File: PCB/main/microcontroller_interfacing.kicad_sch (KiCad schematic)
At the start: 18 parts, among them J5 Conn_01x02_Male, U1 USB_Micro_B, U2 CH340G, U3 AT24C256C-SSHL-T, X1 12MHz Crystal

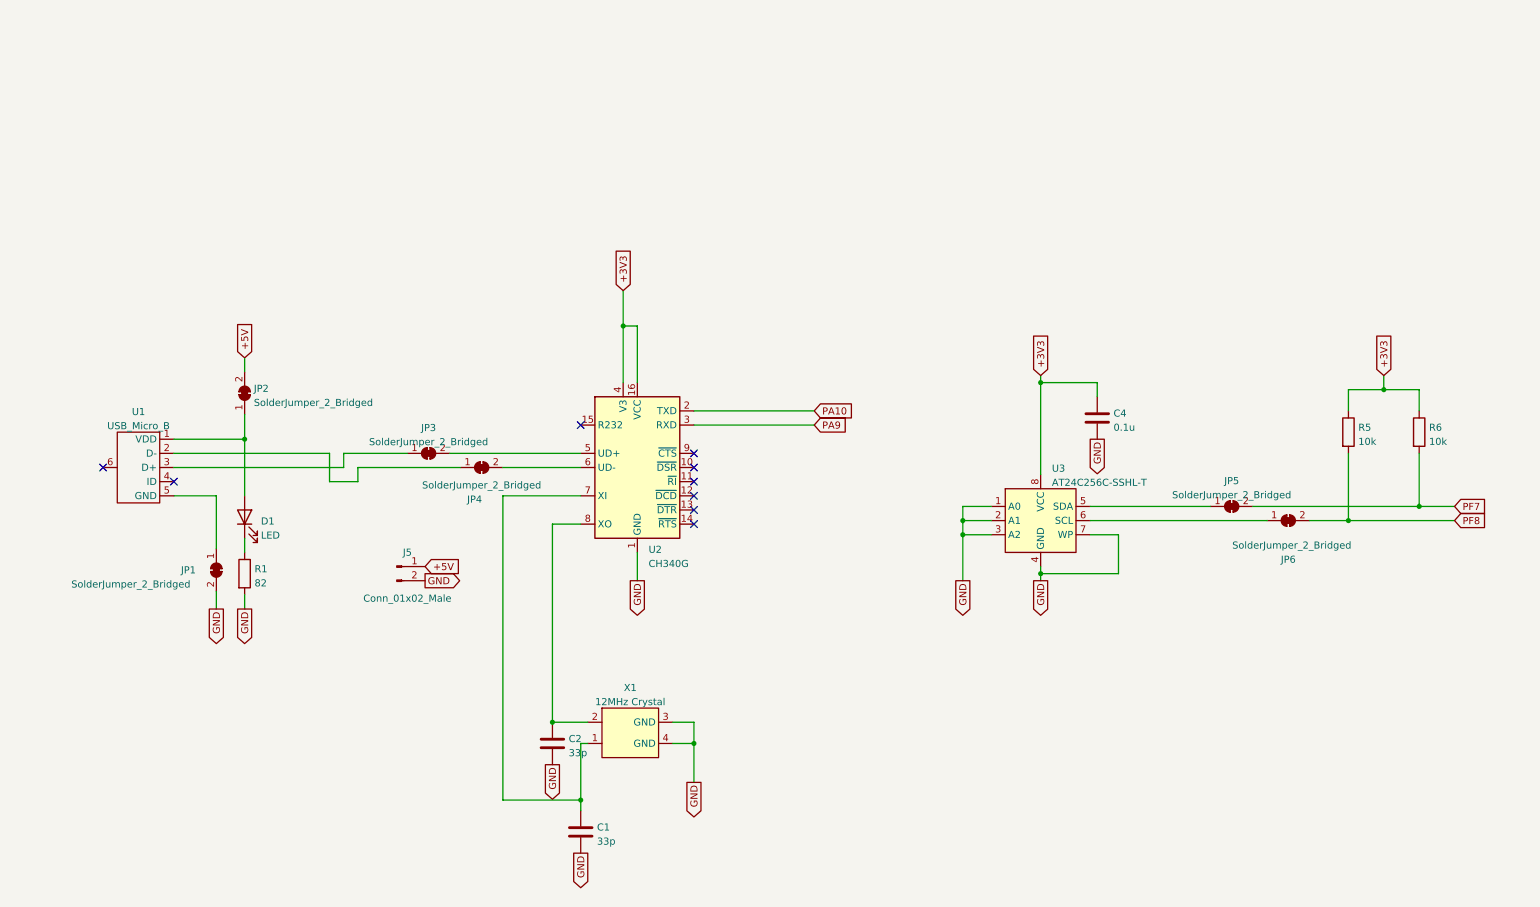
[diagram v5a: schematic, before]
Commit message: Neaten schematic
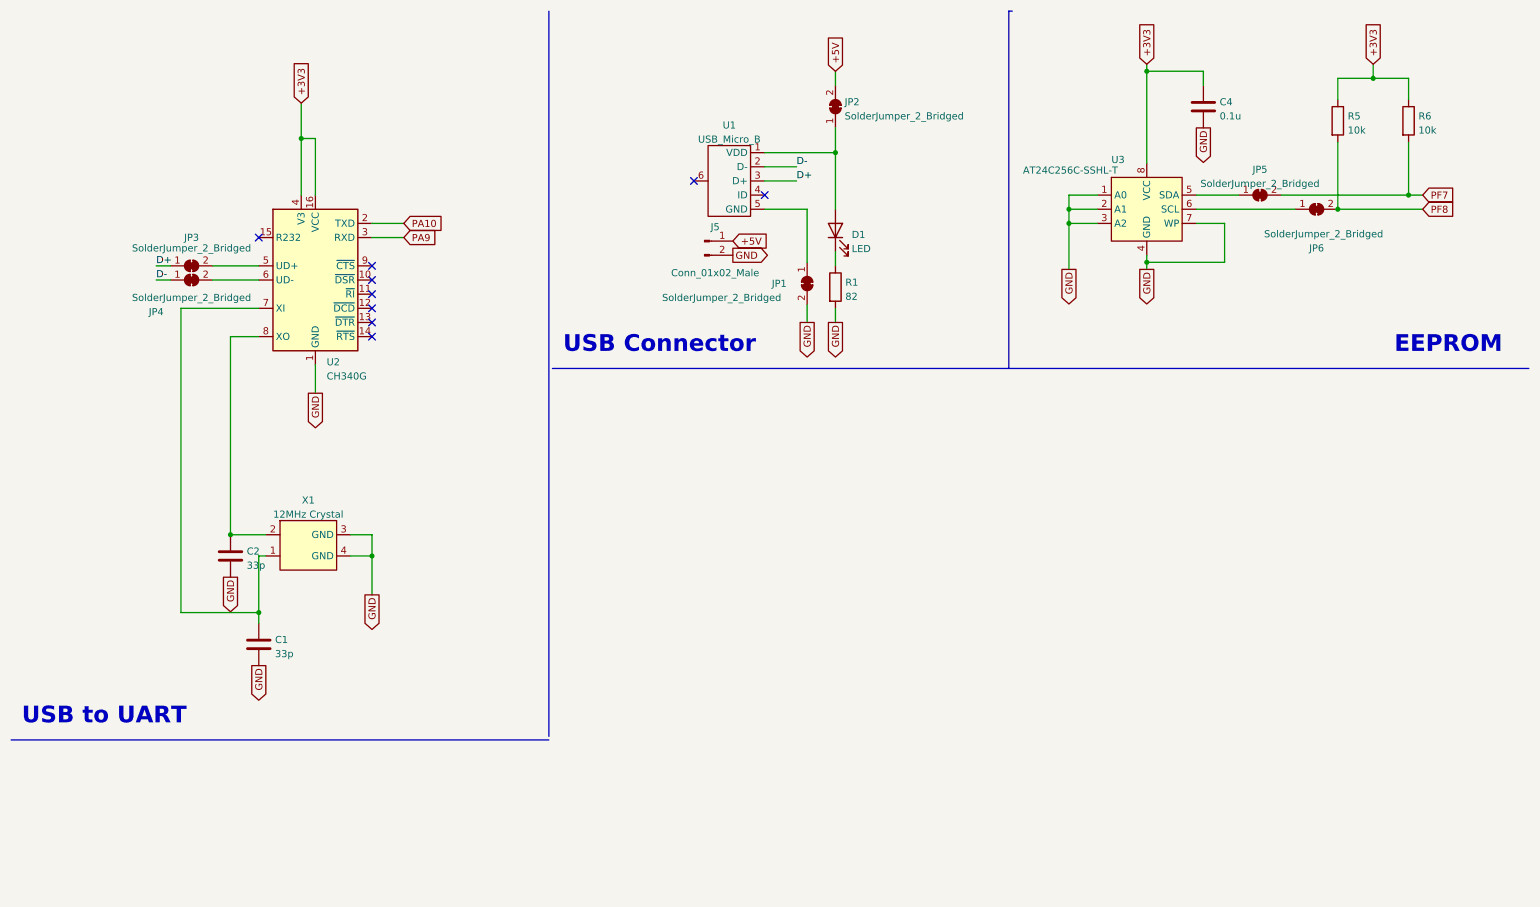
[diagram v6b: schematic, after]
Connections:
- net D-: now reaches JP4.1 (A), U1.2 (D-)
- net D+: now reaches JP3.1 (A), U1.3 (D+)
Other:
- note added: "EEPROM"
- note added: "USB Connector"
- note added: "USB to UART"
- moved on the sheet: C1, C2, C4, D1, J5, JP1, JP2, JP3, JP4, JP5, JP6, R1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

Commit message: Update paths
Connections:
- net PF7 renamed PB7
- net PF8 renamed PB8
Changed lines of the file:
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@@
     )
   )
-  (global_label "PF8" (shape input) (at 265.43 47.625 0) (fields_autoplaced)
+  (global_label "PB8" (shape input) (at 265.43 47.625 0) (fields_autoplaced)
     (effects (font (size 1.27 1.27)) (justify left))
-    (property "Intersheet References" "${INTERSHEET_REFS}" (id 0) (at 271.4112 47.5456 0)
+    (property "Intersheet References" "${INTERSHEET_REFS}" (id 0) (at 271.5926 47.5456 0)
       (effects (font (size 1.27 1.27)) (justify left) hide)
     )
@@
     )
   )
-  (global_label "PF7" (shape input) (at 265.43 45.085 0) (fields_autoplaced)
+  (global_label "PB7" (shape input) (at 265.43 45.085 0) (fields_autoplaced)
     (effects (font (size 1.27 1.27)) (justify left))
-    (property "Intersheet References" "${INTERSHEET_REFS}" (id 0) (at 271.4112 45.0056 0)
+    (property "Intersheet References" "${INTERSHEET_REFS}" (id 0) (at 271.5926 45.0056 0)
       (effects (font (size 1.27 1.27)) (justify left) hide)
     )

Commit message: Change ports
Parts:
- removed J5: Conn_01x02_Male, Connector_PinHeader_1.00mm:PinHeader_1x02_P1.00mm_Vertical, symbol Connector:Conn_01x02_Male
- added J5: Conn_01x02_Female, symbol Connector:Conn_01x02_Female
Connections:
- net +5V: now also J5.2 (Pin_2)
- net GND: now also J5.1 (Pin_1)
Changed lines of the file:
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@@
     )
   )
-  (global_label "+5V" (shape input) (at 141.605 53.34 0) (fields_autoplaced)
+  (global_label "+5V" (shape input) (at 140.335 20.32 0) (fields_autoplaced)
     (effects (font (size 1.27 1.27)) (justify left))
-    (property "Intersheet References" "${INTERSHEET_REFS}" (id 0) (at 147.8886 53.2606 0)
+    (property "Intersheet References" "${INTERSHEET_REFS}" (id 0) (at 146.6186 20.2406 0)
       (effects (font (size 1.27 1.27)) (justify left) hide)
     )
   )
-  (global_label "GND" (shape output) (at 141.605 55.88 0) (fields_autoplaced)
+  (global_label "GND" (shape output) (at 140.335 22.86 0) (fields_autoplaced)
     (effects (font (size 1.27 1.27)) (justify left))
-    (property "Intersheet References" "${INTERSHEET_REFS}" (id 0) (at 147.8886 55.8006 0)
+    (property "Intersheet References" "${INTERSHEET_REFS}" (id 0) (at 146.6186 22.7806 0)
       (effects (font (size 1.27 1.27)) (justify left) hide)
     )
@@
     (pin "2")
   )
+  (symbol (lib_id "Connector:Conn_01x02_Female") (at 135.255 22.86 180) (unit 1)
+    (in_bom yes) (on_board yes)
+    (property "Reference" "J5" (id 0) (at 133.985 17.145 0))
+    (property "Value" "Conn_01x02_Female" (id 1) (at 133.35 26.035 0))
+    (property "Footprint" "" (id 2) (at 135.255 22.86 0)
+      (effects (font (size 1.27 1.27)) hide)
+    )
+    (property "Datasheet" "~" (id 3) (at 135.255 22.86 0)
+      (effects (font (size 1.27 1.27)) hide)
+    )
+    (pin "1")
+    (pin "2")
+  )
   (symbol (lib_id "Device:R") (at 160.02 61.595 0) (unit 1)
     (in_bom yes) (on_board yes) (fields_autoplaced)
@@
       (effects (font (size 1.27 1.27)) hide)
     )
-    (pin "1")
-    (pin "2")
-  )
-  (symbol (lib_id "Connector:Conn_01x02_Male") (at 136.525 53.34 0) (unit 1)
-    (in_bom yes) (on_board yes)
-    (property "Reference" "J5" (id 0) (at 138.43 50.8 0))
-    (property "Value" "Conn_01x02_Male" (id 1) (at 138.43 59.055 0))
-    (property "Footprint" "Connector_PinHeader_1.00mm:PinHeader_1x02_P1.00mm_Vertical" (id 2) (at 136.525 53.34 0)
-      (effects (font (size 1.27 1.27)) hide)
-    )
-    (property "Datasheet" "~" (id 3) (at 136.525 53.34 0)
-      (effects (font (size 1.27 1.27)) hide)
-    )
